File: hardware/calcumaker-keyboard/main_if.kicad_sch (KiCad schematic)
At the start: 1 part, among them J1 TO MCU

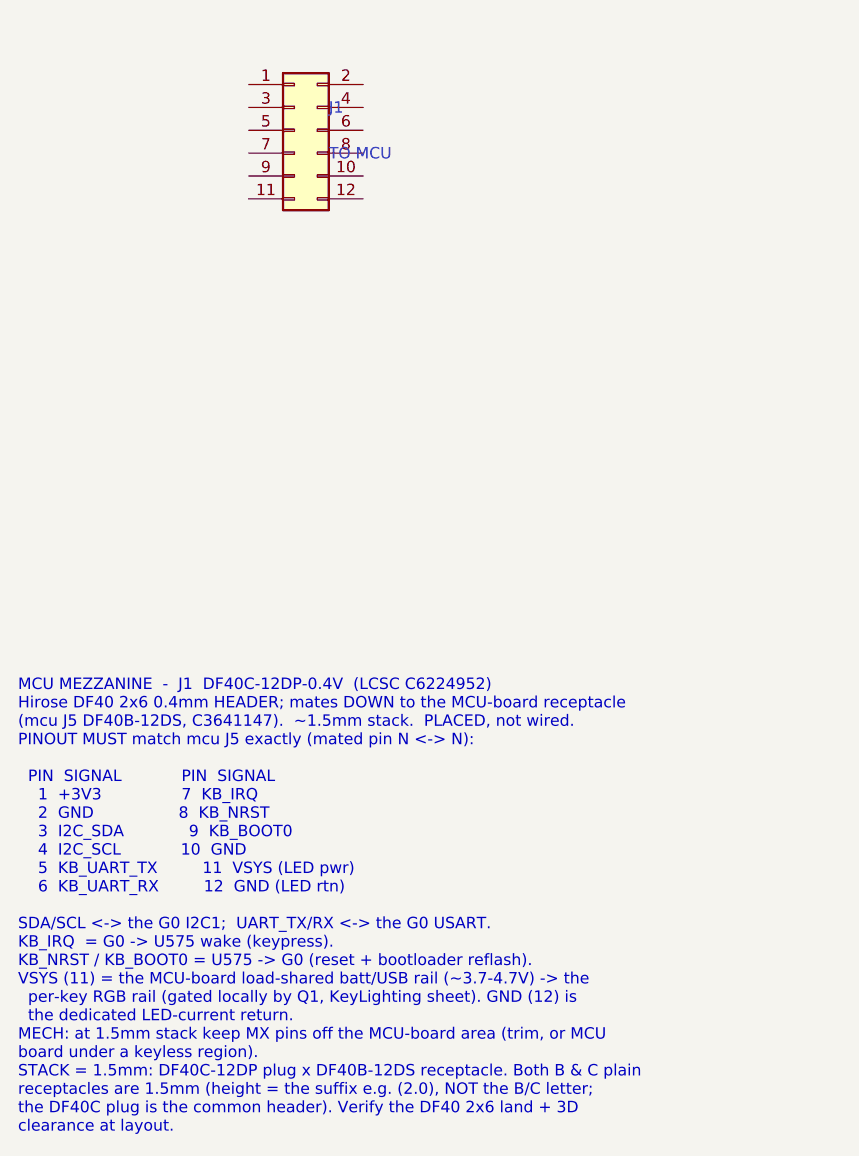
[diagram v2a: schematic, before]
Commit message: hardware: keyboard as a multi-channel design (reusable 10-key row x5) (#5)
Refactor calcumaker-keyboard from a FLAT layout (100 individually-placed SW/D
parts on one sheet + 50 flat RGB LEDs) into a KiCad multi-channel design,
matching the display board.

- key_row.kicad_sch: a reusable 10-key row, FULLY WIRED, instantiated x5
  (Row1-5). Each key = MX switch + 1N4148W diode + SK6805 RGB.
    matrix  SW.1 -> ROW (hier); SW.2 -> KNk -> diode.A; diode.K -> COLk (global)
    RGB     DIN -> LED1..LED10 -> DOUT (hier, chained @root); VDD->VLED, VSS->GND
  Per-instance refs SW1-50 / D1-50 (matrix) / D56-105 (RGB). Shared buses
  (COL1-10, VLED, GND) are global nets; ROW + RGB DIN/DOUT are hierarchical pins
  wired at the root (KB_ROW1-5; KB_LED_DATA -> Row1 -> ... -> Row5 -> RGB_END).
- Split the old KeyLighting sheet -> key_row (the 50 LEDs) + rgb_power (the
  level shifter + gated load switch).
- Converted the whole keyboard manifest from the flat K.build() path to the
  display-style write_wired_child/write_root API; the one-off sheets
  (annunc/kbd_mcu/rgb_power/main_if) stay single-instance, placed via a grid
  helper. Removed the obsolete keypad.kicad_sch + keylight.kicad_sch.
- Docs (DESIGN.md sheet plan, CLAUDE/AGENTS, scripts README) + a few stale fixes
  (STM32U575RGTx, "three boards", current sheet names).

178 components, no duplicate refs, all three boards pass the structure check.
(The 2 lib_symbol_mismatch ERC warnings on the G0/TagConnect are pre-existing
kschgen symbol-cache fidelity, not from this change.)

Co-authored-by: Claude Opus 4.8 (1M context) <noreply@anthropic.com>
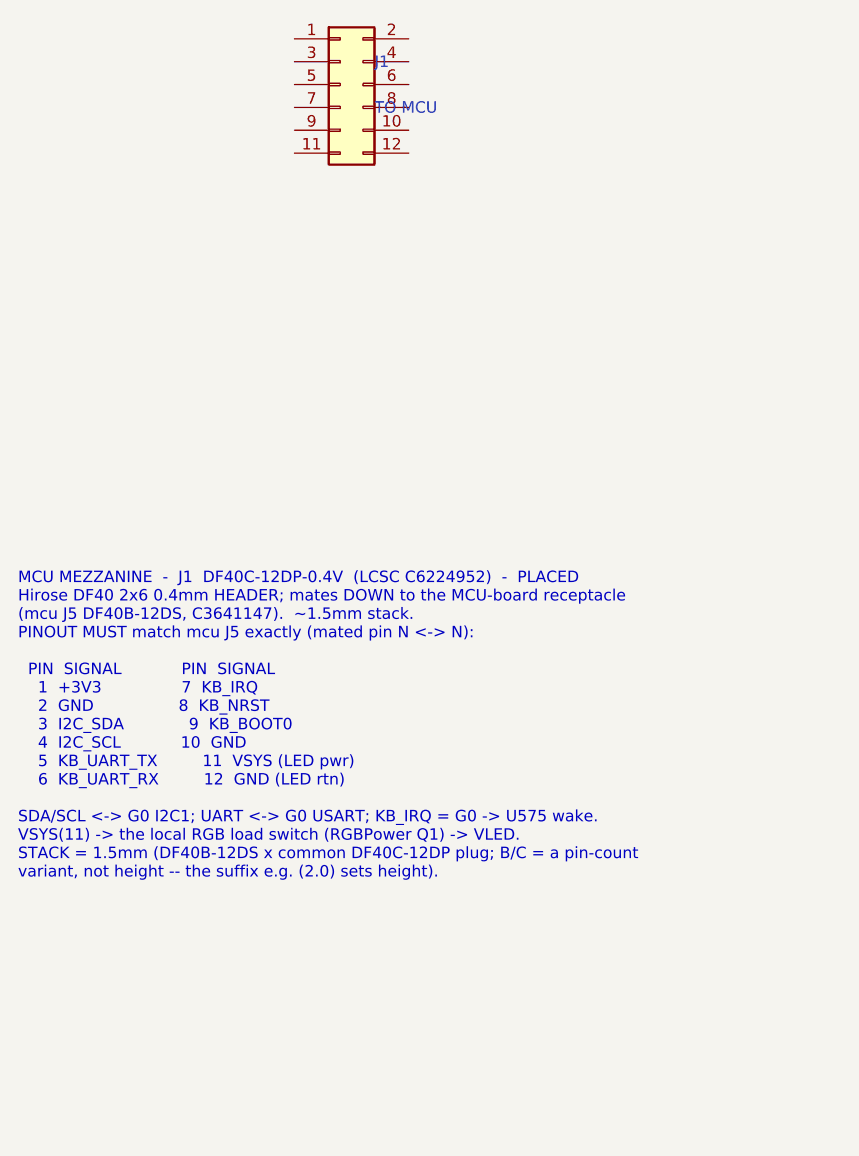
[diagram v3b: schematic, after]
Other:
- note added: "MCU MEZZANINE - J1 DF40C-12DP-0.4V (LCSC C6224952) - PLACED Hirose DF40 2x6 0.4mm HEADER; mates DOWN to the MCU-board receptacle (mcu J5 DF40B-12DS, C3641147). ~1.5mm stack. PINOUT MUST match mcu J5 exactly (mated pin N <-> N): PIN SIGNAL PIN SIGNAL 1 +3V3 7 KB_IRQ 2 GND 8 KB_NRST 3 I2C_SDA 9 KB_BOOT0 4 I2C_SCL 10 GND 5 KB_UART_TX 11 VSYS (LED pwr) 6 KB_UART_RX 12 GND (LED rtn) SDA/SCL <-> G0 I2C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"
- note removed: "MCU MEZZANINE - J1 DF40C-12DP-0.4V (LCSC C6224952) Hirose DF40 2x6 0.4mm HEADER; mates DOWN to the MCU-board receptacle (mcu J5 DF40B-12DS, C3641147). ~1.5mm stack. PLACED, not wired. PINOUT MUST match mcu J5 exactly (mated pin N <-> N): PIN SIGNAL PIN SIGNAL 1 +3V3 7 KB_IRQ 2 GND 8 KB_NRST 3 I2C_SDA 9 KB_BOOT0 4 I2C_SCL 10 GND 5 KB_UART_TX 11 VSYS (LED pwr) 6 KB_UART_RX 12 GND (LED rtn) SDA/SCL 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"
- title: Calcumaker 16 — Keyboard — MCU mezzanine (I2C + UART + VSYS down to the MCU board) -> Calcumaker 16 — Keyboard — MCU mezzanine (I2C + UART + VSYS to the MCU board)
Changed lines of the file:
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@@
 	(paper "A3")
 	(title_block
-		(title "Calcumaker 16 — Keyboard — MCU mezzanine (I2C + UART + VSYS down to the MCU board)")
+		(title "Calcumaker 16 — Keyboard — MCU mezzanine (I2C + UART + VSYS to the MCU board)")
 		(date "2026-07-06")
-		(rev "0.3")
+		(rev "0.4")
 		(company "calcumaker authors")
 	)
 	(symbol
 		(lib_id "Connector_Generic:Conn_02x06_Odd_Even")
-		(at 45.7200 55.8800 0)
+		(at 50.8000 50.8000 0)
 		(unit 1)
 		(exclude_from_sim no)
@@
 		(dnp no)
 		(property "Reference" "J1"
-			(at 49.5300 53.3400 0)
+			(at 54.6100 48.2600 0)
 			(effects (font (size 1.27 1.27)) (justify left))
 		)
 		(property "Value" "TO MCU"
-			(at 49.5300 58.4200 0)
+			(at 54.6100 53.3400 0)
 			(effects (font (size 1.27 1.27)) (justify left))
 		)
 		(property "Footprint" "Connector_Hirose_DF40:Hirose_DF40C-12DP-0.4V_2x06-1MP_P0.4mm"
-			(at 45.7200 55.8800 0)
+			(at 50.8000 50.8000 0)
 			(effects (font (size 1.27 1.27))) (hide yes)
 		)
 		(property "Datasheet" "~"
-			(at 45.7200 55.8800 0)
+			(at 50.8000 50.8000 0)
 			(effects (font (size 1.27 1.27))) (hide yes)
 		)
 		(property "LCSC" "C6224952"
-			(at 45.7200 55.8800 0)
+			(at 50.8000 50.8000 0)
 			(effects (font (size 1.27 1.27))) (hide yes)
 		)
 		(property "MPN" "DF40C-12DP-0.4V(51)"
-			(at 45.7200 55.8800 0)
+			(at 50.8000 50.8000 0)
 			(effects (font (size 1.27 1.27))) (hide yes)
 		)
 		(property "Manufacturer" "Hirose"
-			(at 45.7200 55.8800 0)
+			(at 50.8000 50.8000 0)
 			(effects (font (size 1.27 1.27))) (hide yes)
 		)
@@
 		(instances
 			(project "calcumaker-keyboard"
-				(path "/ca1c0000-0000-4000-8000-00000000eb01/b7ee0e1e-9650-4819-94f9-be2379d6e47b"
+				(path "/ca1c0000-0000-4000-8000-00000000eb01/ca1c0000-0000-4000-8000-00000000eb50"
 					(reference "J1")
 					(unit 1)
@@
 		)
 	)
-	(text "MCU MEZZANINE  -  J1  DF40C-12DP-0.4V  (LCSC C6224952)\nHirose DF40 2x6 0.4mm HEADER; mates DOWN to the MCU-board receptacle\n(mcu J5 DF40B-12DS, C3641147).  ~1.5mm stack.  PLACED, not wired.\nPINOUT MUST match mcu J5 exactly (mated pin N <-> N):\n\n  PIN  SIGNAL            PIN  SIGNAL        \n    1  +3V3                7  KB_IRQ        \n    2  GND                 8  KB_NRST       \n    3  I2C_SDA             9  KB_BOOT0      \n    4  I2C_SCL            10  GND           \n    5  KB_UART_TX         11  VSYS (LED pwr)\n    6  KB_UART_RX         12  GND (LED rtn)\n\nSDA/SCL <-> the G0 I2C1;  UART_TX/RX <-> the G0 USART.\nKB_IRQ  = G0 -> U575 wake (keypress).\nKB_NRST / KB_BOOT0 = U575 -> G0 (reset + bootloader reflash).\nVSYS (11) = the MCU-board load-shared batt/USB rail (~3.7-4.7V) -> the\n  per-key RGB rail (gated locally by Q1, KeyLighting sheet). GND (12) is\n  the dedicated LED-current return.\nMECH: at 1.5mm stack keep MX pins off the MCU-board area (trim, or MCU\nboard under a keyless region).\nSTACK = 1.5mm: DF40C-12DP plug x DF40B-12DS receptacle. Both B & C plain\nreceptacles are 1.5mm (height = the suffix e.g. (2.0), NOT the B/C letter;\nthe DF40C plug is the common header). Verify the DF40 2x6 land + 3D\nclearance at layout."
+	(text "MCU MEZZANINE  -  J1  DF40C-12DP-0.4V  (LCSC C6224952)  -  PLACED\nHirose DF40 2x6 0.4mm HEADER; mates DOWN to the MCU-board receptacle\n(mcu J5 DF40B-12DS, C3641147).  ~1.5mm stack.\nPINOUT MUST match mcu J5 exactly (mated pin N <-> N):\n\n  PIN  SIGNAL            PIN  SIGNAL        \n    1  +3V3                7  KB_IRQ        \n    2  GND                 8  KB_NRST       \n    3  I2C_SDA             9  KB_BOOT0      \n    4  I2C_SCL            10  GND           \n    5  KB_UART_TX         11  VSYS (LED pwr)\n    6  KB_UART_RX         12  GND (LED rtn)\n\nSDA/SCL <-> G0 I2C1; UART <-> G0 USART; KB_IRQ = G0 -> U575 wake.\nVSYS(11) -> the local RGB load switch (RGBPower Q1) -> VLED.\nSTACK = 1.5mm (DF40B-12DS x common DF40C-12DP plug; B/C = a pin-count\nvariant, not height -- the suffix e.g. (2.0) sets height)."
 		(exclude_from_sim no)
-		(at 15.00 116.88 0)
+		(at 15.00 105.00 0)
 		(effects (font (face "Courier New") (size 1.27 1.27)) (justify left top))
 	)

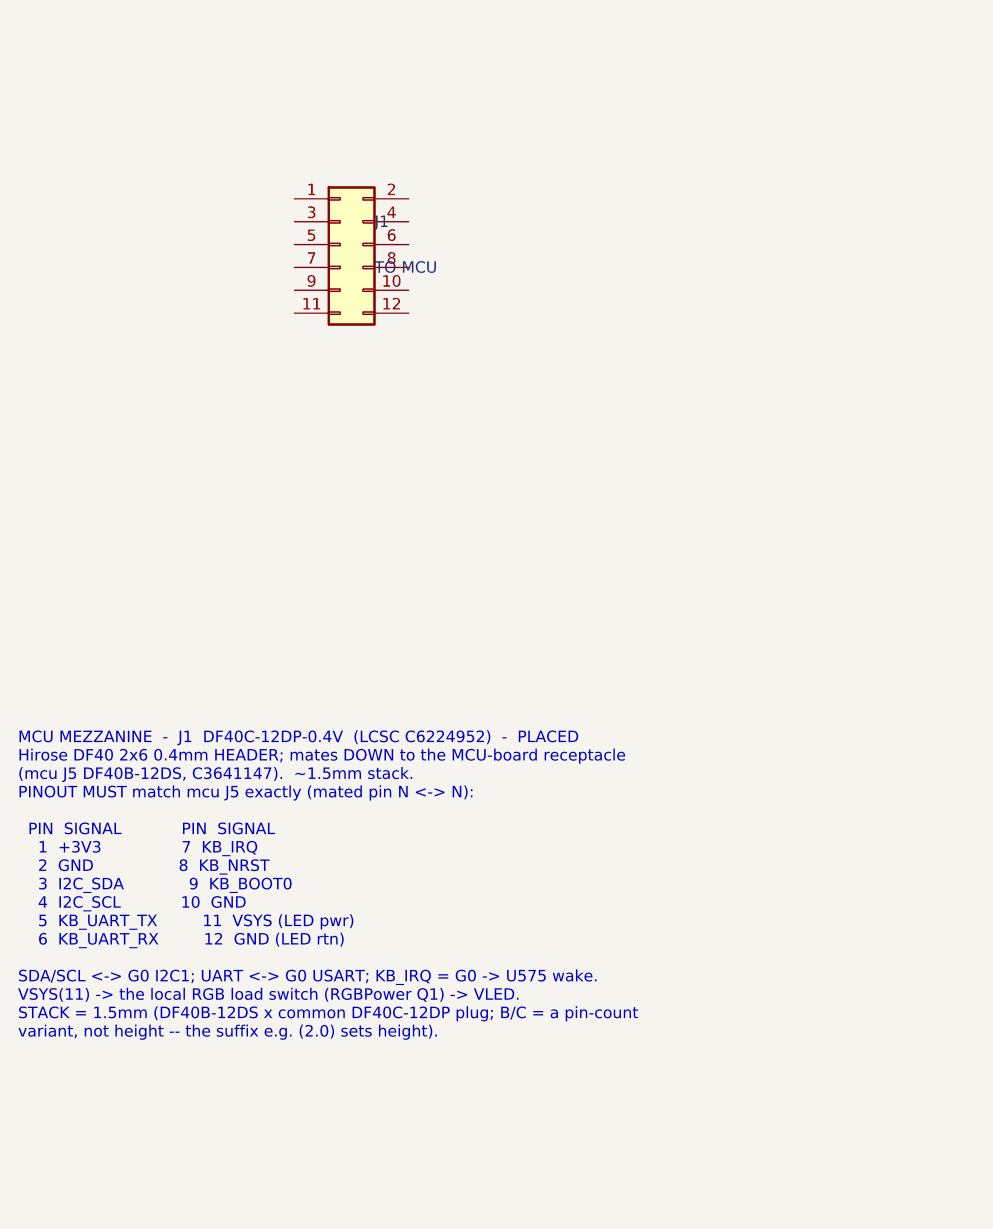
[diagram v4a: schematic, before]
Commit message: hardware: schematic wiring + design/parts updates (WIP)
Pre-existing working-tree changes across the MCU and keyboard boards: wiring
build-out on the mezzanine interfaces (main_if / keyboard_if), MCU/PSU/display/
clock/QSPI sheet edits, per-key row updates, plus DESIGN.md, PARTS.md, and the
two schgen manifests. Committed as-is at the user's request.

Co-Authored-By: Claude Opus 4.8 (1M context) <noreply@anthropic.com>
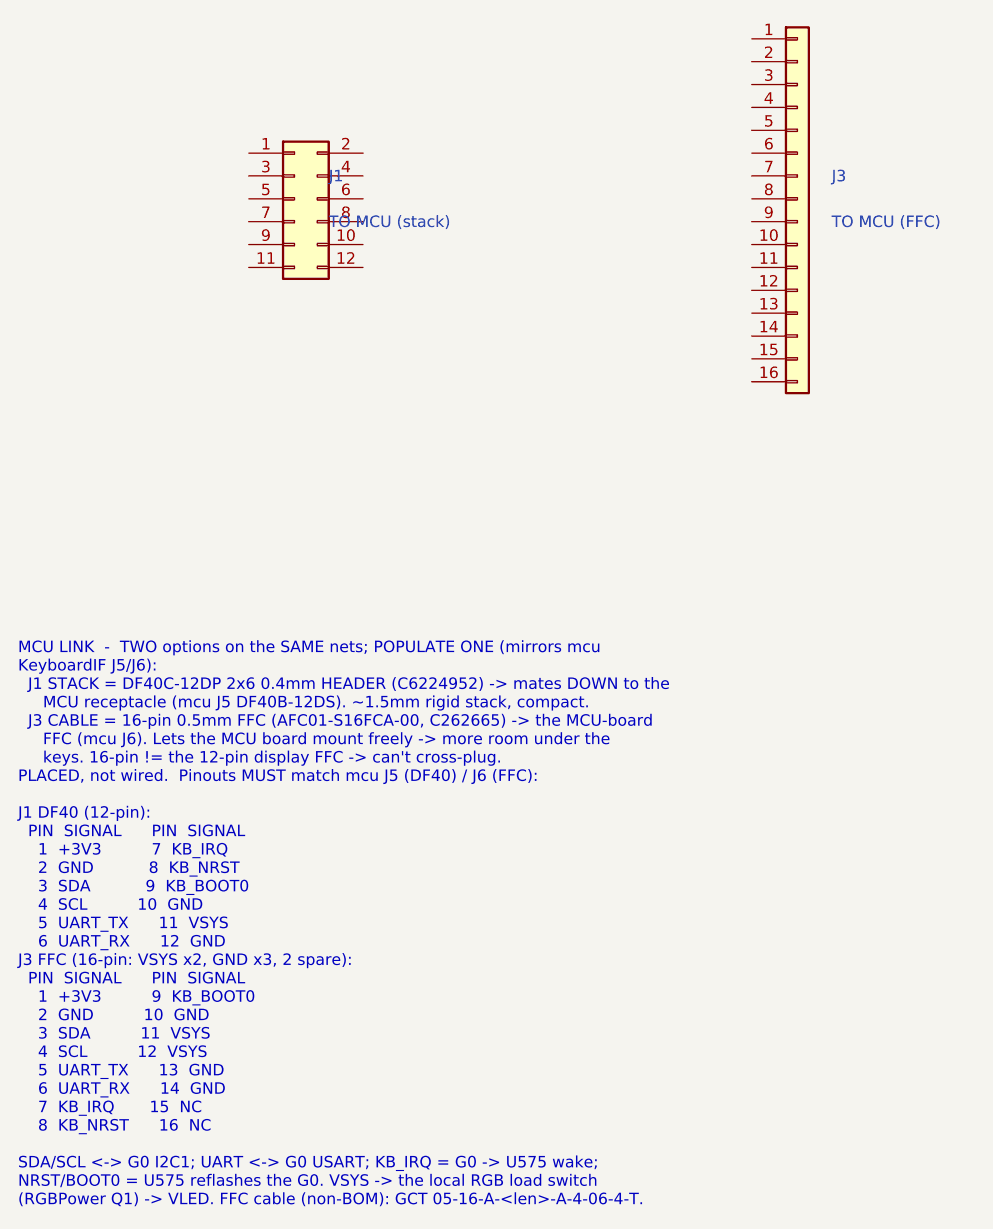
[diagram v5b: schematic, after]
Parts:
- added J3: TO MCU (FFC), Connector_FFC-FPC:Hirose_FH12-16S-0.5SH_1x16-1MP_P0.50mm_Horizontal, symbol Connector_Generic:Conn_01x16
- J1: value TO MCU -> TO MCU (stack)
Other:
- note added: "MCU LINK - TWO options on the SAME nets; POPULATE ONE (mirrors mcu KeyboardIF J5/J6): J1 STACK = DF40C-12DP 2x6 0.4mm HEADER (C6224952) -> mates DOWN to the MCU receptacle (mcu J5 DF40B-12DS). ~1.5mm rigid stack, compact. J3 CABLE = 16-pin 0.5mm FFC (AFC01-S16FCA-00, C262665) -> the MCU-board FFC (mcu J6). Lets the MCU board mount freely -> more room under the keys. 16-pin != the 12-pin display F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"
- note removed: "MCU MEZZANINE - J1 DF40C-12DP-0.4V (LCSC C6224952) - PLACED Hirose DF40 2x6 0.4mm HEADER; mates DOWN to the MCU-board receptacle (mcu J5 DF40B-12DS, C3641147). ~1.5mm stack. PINOUT MUST match mcu J5 exactly (mated pin N <-> N): PIN SIGNAL PIN SIGNAL 1 +3V3 7 KB_IRQ 2 GND 8 KB_NRST 3 I2C_SDA 9 KB_BOOT0 4 I2C_SCL 10 GND 5 KB_UART_TX 11 VSYS (LED pwr) 6 KB_UART_RX 12 GND (LED rtn) SDA/SCL <-> G0 I2C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"
- title: Calcumaker 16 — Keyboard — MCU mezzanine (I2C + UART + VSYS to the MCU board) -> Calcumaker 16 — Keyboard — MCU link -- DF40 stack (J1) OR 16-pin FFC (J3), populate one
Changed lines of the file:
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@@
 	(paper "A3")
 	(title_block
-		(title "Calcumaker 16 — Keyboard — MCU mezzanine (I2C + UART + VSYS to the MCU board)")
+		(title "Calcumaker 16 — Keyboard — MCU link -- DF40 stack (J1) OR 16-pin FFC (J3), populate one")
 		(date "2026-07-06")
 		(rev "0.4")
@@
 	(symbol
 		(lib_id "Connector_Generic:Conn_02x06_Odd_Even")
-		(at 50.8000 50.8000 0)
+		(at 45.7200 45.7200 0)
 		(unit 1)
 		(exclude_from_sim no)
@@
 		(dnp no)
 		(property "Reference" "J1"
-			(at 54.6100 48.2600 0)
+			(at 49.5300 43.1800 0)
 			(effects (font (size 1.27 1.27)) (justify left))
 		)
-		(property "Value" "TO MCU"
-			(at 54.6100 53.3400 0)
+		(property "Value" "TO MCU (stack)"
+			(at 49.5300 48.2600 0)
 			(effects (font (size 1.27 1.27)) (justify left))
 		)
 		(property "Footprint" "Connector_Hirose_DF40:Hirose_DF40C-12DP-0.4V_2x06-1MP_P0.4mm"
-			(at 50.8000 50.8000 0)
+			(at 45.7200 45.7200 0)
 			(effects (font (size 1.27 1.27))) (hide yes)
 		)
 		(property "Datasheet" "~"
-			(at 50.8000 50.8000 0)
+			(at 45.7200 45.7200 0)
 			(effects (font (size 1.27 1.27))) (hide yes)
 		)
 		(property "LCSC" "C6224952"
-			(at 50.8000 50.8000 0)
+			(at 45.7200 45.7200 0)
 			(effects (font (size 1.27 1.27))) (hide yes)
 		)
 		(property "MPN" "DF40C-12DP-0.4V(51)"
-			(at 50.8000 50.8000 0)
+			(at 45.7200 45.7200 0)
 			(effects (font (size 1.27 1.27))) (hide yes)
 		)
 		(property "Manufacturer" "Hirose"
-			(at 50.8000 50.8000 0)
+			(at 45.7200 45.7200 0)
 			(effects (font (size 1.27 1.27))) (hide yes)
 		)
@@
 		)
 	)
-	(text "MCU MEZZANINE  -  J1  DF40C-12DP-0.4V  (LCSC C6224952)  -  PLACED\nHirose DF40 2x6 0.4mm HEADER; mates DOWN to the MCU-board receptacle\n(mcu J5 DF40B-12DS, C3641147).  ~1.5mm stack.\nPINOUT MUST match mcu J5 exactly (mated pin N <-> N):\n\n  PIN  SIGNAL            PIN  SIGNAL        \n    1  +3V3                7  KB_IRQ        \n    2  GND                 8  KB_NRST       \n    3  I2C_SDA             9  KB_BOOT0      \n    4  I2C_SCL            10  GND           \n    5  KB_UART_TX         11  VSYS (LED pwr)\n    6  KB_UART_RX         12  GND (LED rtn)\n\nSDA/SCL <-> G0 I2C1; UART <-> G0 USART; KB_IRQ = G0 -> U575 wake.\nVSYS(11) -> the local RGB load switch (RGBPower Q1) -> VLED.\nSTACK = 1.5mm (DF40B-12DS x common DF40C-12DP plug; B/C = a pin-count\nvariant, not height -- the suffix e.g. (2.0) sets height)."
+	(symbol
+		(lib_id "Connector_Generic:Conn_01x16")
+		(at 101.6000 45.7200 0)
+		(unit 1)
 		(exclude_from_sim no)
-		(at 15.00 105.00 0)
+		(in_bom yes)
+		(on_board yes)
+		(dnp no)
+		(property "Reference" "J3"
+			(at 105.4100 43.1800 0)
+			(effects (font (size 1.27 1.27)) (justify left))
+		)
+		(property "Value" "TO MCU (FFC)"
+			(at 105.4100 48.2600 0)
+			(effects (font (size 1.27 1.27)) (justify left))
+		)
+		(property "Footprint" "Connector_FFC-FPC:Hirose_FH12-16S-0.5SH_1x16-1MP_P0.50mm_Horizontal"
+			(at 101.6000 45.7200 0)
+			(effects (font (size 1.27 1.27))) (hide yes)
+		)
+		(property "Datasheet" "~"
+			(at 101.6000 45.7200 0)
+			(effects (font (size 1.27 1.27))) (hide yes)
+		)
+		(property "LCSC" "C262665"
+			(at 101.6000 45.7200 0)
+			(effects (font (size 1.27 1.27))) (hide yes)
+		)
+		(property "MPN" "AFC01-S16FCA-00"
+			(at 101.6000 45.7200 0)
+			(effects (font (size 1.27 1.27))) (hide yes)
+		)
+		(property "Manufacturer" "JUSHUO"
+			(at 101.6000 45.7200 0)
+			(effects (font (size 1.27 1.27))) (hide yes)
+		)
+		(pin "1")
+		(pin "2")
+		(pin "3")
+		(pin "4")
+		(pin "5")
+		(pin "6")
+		(pin "7")
+		(pin "8")
+		(pin "9")
+		(pin "10")
+		(pin "11")
+		(pin "12")
+		(pin "13")
+		(pin "14")
+		(pin "15")
+		(pin "16")
+		(instances
+			(project "calcumaker-keyboard"
+				(path "/ca1c0000-0000-4000-8000-00000000eb01/ca1c0000-0000-4000-8000-00000000eb50"
+					(reference "J3")
+					(unit 1)
+				)
+			)
+		)
+	)
+	(text "MCU LINK  -  TWO options on the SAME nets; POPULATE ONE (mirrors mcu\nKeyboardIF J5/J6):\n  J1 STACK = DF40C-12DP 2x6 0.4mm HEADER (C6224952) -> mates DOWN to the\n     MCU receptacle (mcu J5 DF40B-12DS). ~1.5mm rigid stack, compact.\n  J3 CABLE = 16-pin 0.5mm FFC (AFC01-S16FCA-00, C262665) -> the MCU-board\n     FFC (mcu J6). Lets the MCU board mount freely -> more room under the\n     keys. 16-pin != the 12-pin display FFC -> can't cross-plug.\nPLACED, not wired.  Pinouts MUST match mcu J5 (DF40) / J6 (FFC):\n\nJ1 DF40 (12-pin):\n  PIN  SIGNAL      PIN  SIGNAL  \n    1  +3V3          7  KB_IRQ  \n    2  GND           8  KB_NRST \n    3  SDA           9  KB_BOOT0\n    4  SCL          10  GND     \n    5  UART_TX      11  VSYS    \n    6  UART_RX      12  GND\nJ3 FFC (16-pin: VSYS x2, GND x3, 2 spare):\n  PIN  SIGNAL      PIN  SIGNAL  \n    1  +3V3          9  KB_BOOT0\n    2  GND          10  GND     \n    3  SDA          11  VSYS    \n    4  SCL          12  VSYS    \n    5  UART_TX      13  GND     \n    6  UART_RX      14  GND     \n    7  KB_IRQ       15  NC      \n    8  KB_NRST      16  NC\n\nSDA/SCL <-> G0 I2C1; UART <-> G0 USART; KB_IRQ = G0 -> U575 wake;\nNRST/BOOT0 = U575 reflashes the G0. VSYS -> the local RGB load switch\n(RGBPower Q1) -> VLED. FFC cable (non-BOM): GCT 05-16-A-<len>-A-4-06-4-T."
+		(exclude_from_sim no)
+		(at 15.00 95.00 0)
 		(effects (font (face "Courier New") (size 1.27 1.27)) (justify left top))
 	)
